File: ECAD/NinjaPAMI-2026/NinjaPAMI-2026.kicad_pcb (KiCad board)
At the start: 2 copper layers, 108 x 74 mm, 103 parts, among them J1 Con_Batt, J10 CON_EV_01, J11 Conn_01x04, J12 OLED, J13 RightMotor, J14 LeftMotor, J2 Servo, J3 Servo, J4 Sensor_RIGHT, J5 Sensor_Center, J6 Sensor_LEFT, J7 CON_EV_02, J8 CON_EV_02, J9 CON_PUMP_01, Q1 AO3400A, Q2 AO3400A, Q3 AO3400A, Q4 AO3400A, SW1 SW_SPDT, SW2 SW_Reed, SW3 SW_SPDT, U1 R-78E5.0-1.0, U2 XIAO-HALF-HOLE-23P, U3 TMC2209_SILENTSTEPSTICK, U4 TMC2209_SILENTSTEPSTICK

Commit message: placement pump and ev
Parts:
- C3, C4, J11: moved to B.Cu
- J12: footprint Connector_PinSocket_2.54mm:PinSocket_1x04_P2.54mm_Vertical -> Connector_Molex:Molex_KK-254_AE-6410-04A_1x04_P2.54mm_Vertical; moved to B.Cu
- moved kibuzzard-670C05E9 172.6 mm to (270.4, 106.2)
- moved kibuzzard-670C060B 159.6 mm to (267.4, 106.0)
- moved kibuzzard-670C0614 159.6 mm to (264.9, 105.7)
- moved kibuzzard-670C0418 154.9 mm to (273.9, 106.2)
- moved kibuzzard-670C0436 154.9 mm to (276.4, 106.2)
- moved kibuzzard-670C04A5 143.4 mm to (251.9, 93.2)
- moved G*** 143.4 mm to (254.5, 88.5)
- moved G*** 128.1 mm to (243.2, 93.4)
- moved G*** 109.4 mm to (247.0, 93.5)
- moved G*** 104.2 mm to (254.0, 104.5)
- moved kibuzzard-670C04A5 100.3 mm to (244.0, 89.5)
- moved G*** 100.3 mm to (241.4, 86.3)
- moved kibuzzard-670C23C9 100.0 mm to (258.0, 113.2)
- moved D10 94.9 mm to (168.0, 87.4)
- moved G*** 94.3 mm to (248.5, 88.8)
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
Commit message: modify ARU
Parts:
- removed SW1: SW_SPDT, PAMI-2025:UB16SKW03N-C
- added J15: BAU, Connector_Molex:Molex_KK-396_A-41791-0002_1x02_P3.96mm_Vertical, F.Cu at (116.4, 106.9)
- moved D10 37.2 mm to (205.2, 87.4)
- moved D11 37.2 mm to (205.2, 111.7)
- moved D14 37.2 mm to (214.5, 107.2)
- moved D3 37.2 mm to (205.3, 99.5)
- moved D4 37.2 mm to (214.5, 95.0)
- moved D6 37.2 mm to (205.0, 124.2)
- moved D7 37.2 mm to (214.2, 119.7)
- moved J10 37.2 mm to (220.0, 106.2)
- moved JP2 37.2 mm to (210.7, 97.5)
- moved JP3 37.2 mm to (210.5, 122.2)
- moved JP6 37.2 mm to (210.7, 109.7)
- moved Q1 37.2 mm to (210.3, 92.5)
- moved Q2 37.2 mm to (210.0, 117.2)
- moved Q4 37.2 mm to (210.2, 104.7)
- moved R10 37.2 mm to (204.0, 93.0)
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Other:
- outline, holes or cut-outs redrawn

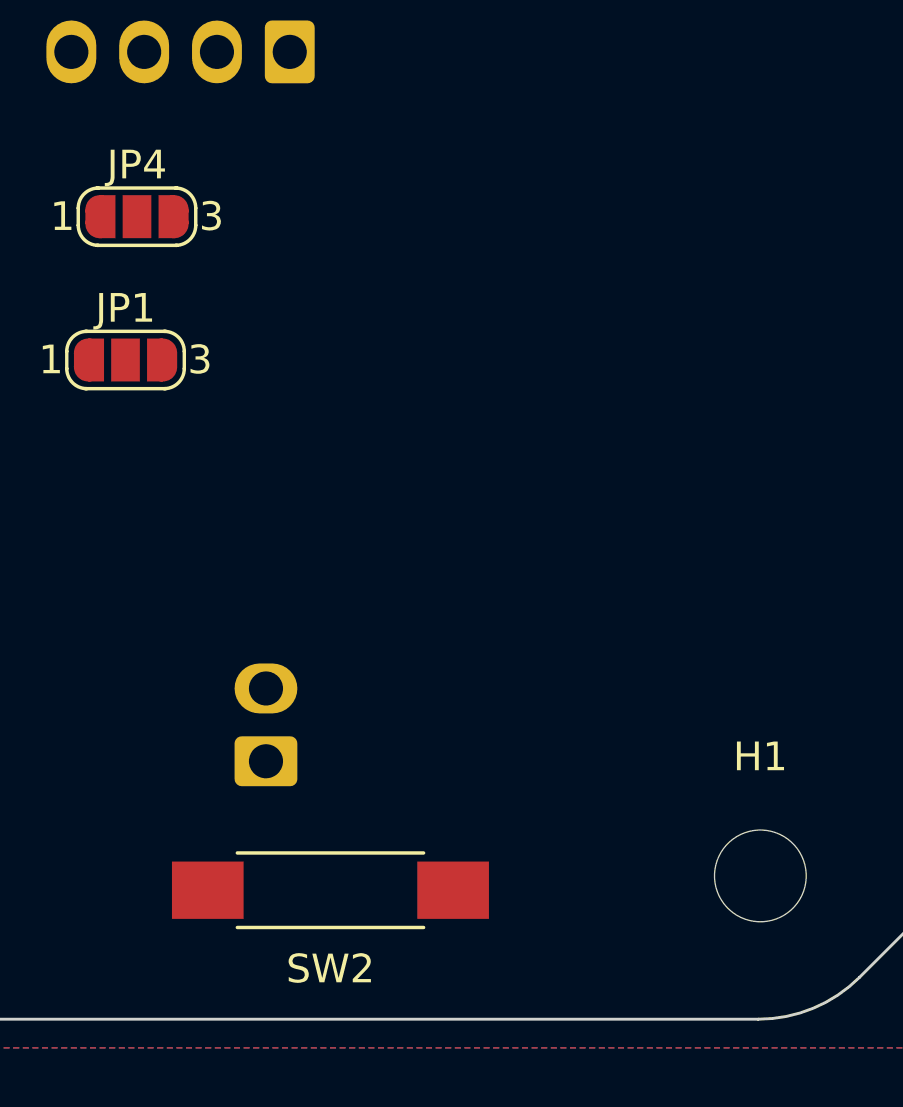
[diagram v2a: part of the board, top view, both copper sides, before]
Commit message: add hall effect sensor
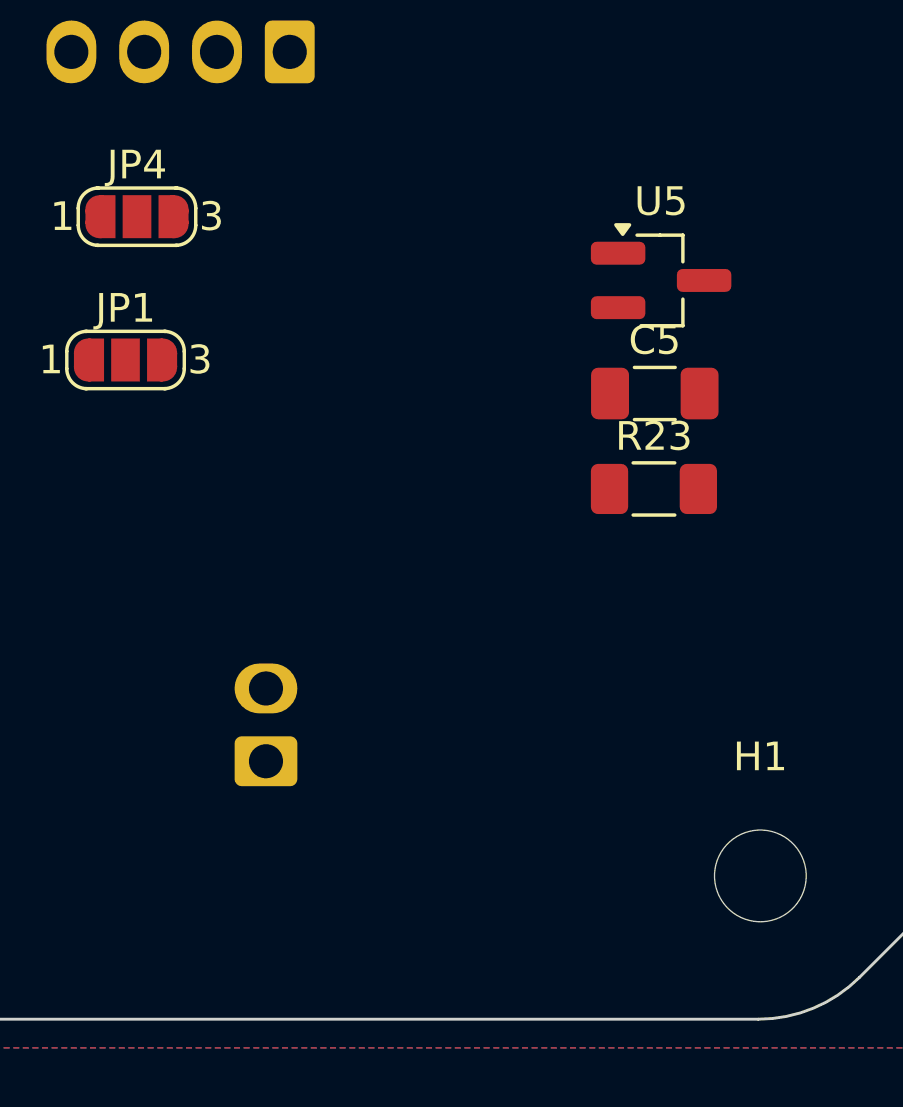
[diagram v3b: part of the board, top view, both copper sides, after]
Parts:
- removed SW2: SW_Reed, Button_Switch_SMD:SW_SPST_REED_CT05-XXXX-G1
- added C5: 0.1uF, Capacitor_SMD:C_1206_3216Metric_Pad1.33x1.80mm_HandSolder, F.Cu at (171.3, 117.2)
- added R23: 10K, Resistor_SMD:R_1206_3216Metric_Pad1.30x1.75mm_HandSolder, F.Cu at (171.3, 120.5)
- added U5: DRV5023, Package_TO_SOT_SMD:SOT-23_Handsoldering, F.Cu at (171.5, 113.2)

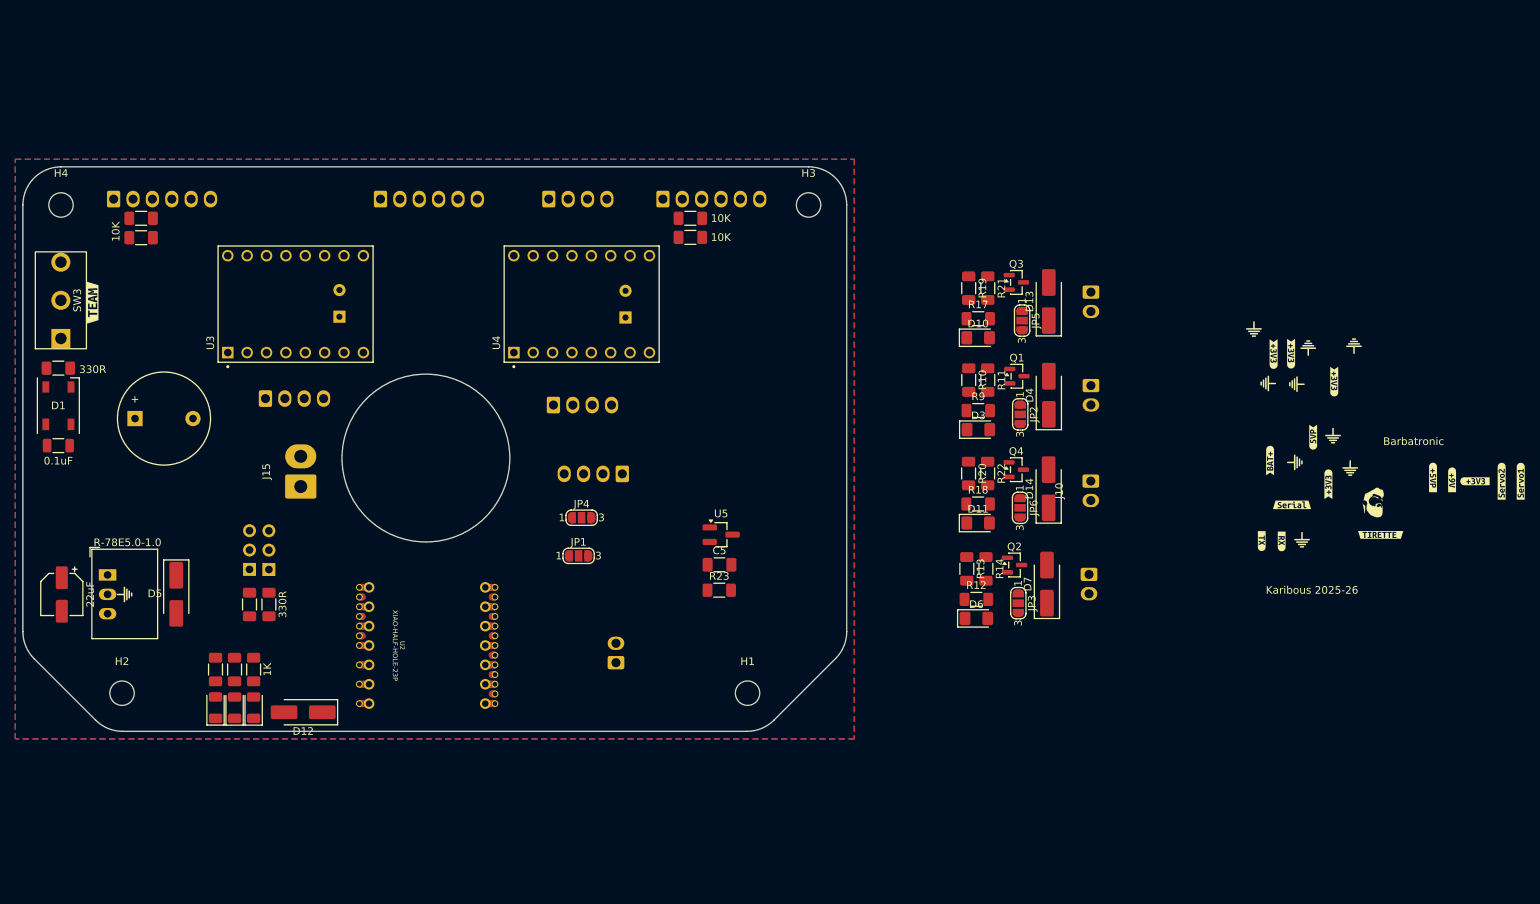
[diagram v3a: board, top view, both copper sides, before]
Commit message: size refactor - add 2.0 regulator
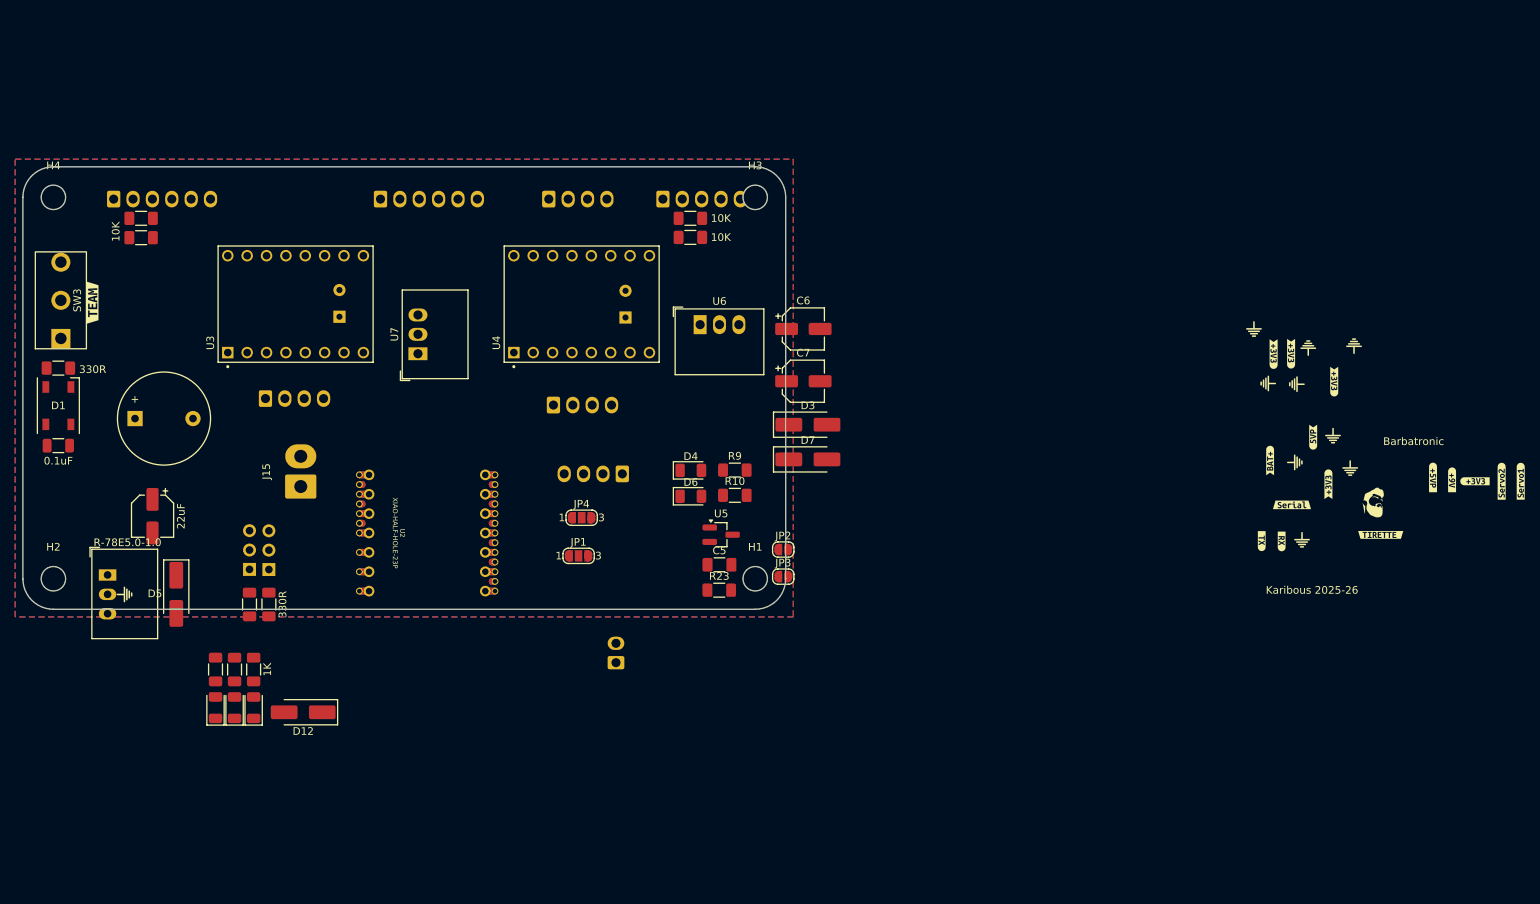
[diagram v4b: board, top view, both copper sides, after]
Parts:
- removed D10, D11: LED_Small, LED_SMD:LED_1206_3216Metric_Pad1.42x1.75mm_HandSolder
- removed D13, D14: D_Small, Diode_SMD:D_SMA_Handsoldering
- removed J10: CON_EV_01, Connector_Molex:Molex_KK-254_AE-6410-02A_1x02_P2.54mm_Vertical
- removed J7, J8: CON_EV_02, Connector_Molex:Molex_KK-254_AE-6410-02A_1x02_P2.54mm_Vertical
- removed J9: CON_PUMP_01, Connector_Molex:Molex_KK-254_AE-6410-02A_1x02_P2.54mm_Vertical
- removed JP5, JP6: SolderJumper_3_Open, Jumper:SolderJumper-3_P1.3mm_Open_RoundedPad1.0x1.5mm_NumberLabels
- removed Q1, Q2, Q3, Q4: AO3400A, Package_TO_SOT_SMD:SOT-23
- removed R11, R14, R21, R22: 10K, Resistor_SMD:R_1206_3216Metric_Pad1.30x1.75mm_HandSolder
- removed R12, R17, R18: 1K, Resistor_SMD:R_1206_3216Metric_Pad1.30x1.75mm_HandSolder
- removed R13, R19, R20: 270R, Resistor_SMD:R_1206_3216Metric_Pad1.30x1.75mm_HandSolder
- added C6: 22uF, Capacitor_SMD:CP_Elec_5x5.4, F.Cu at (182.3, 86.3)
- added C7: 22uF, Capacitor_SMD:CP_Elec_5x5.4, F.Cu at (182.3, 93.1)
- added U6: R-78B5.0-2.0, Converter_DCDC:Converter_DCDC_RECOM_R-78B-2.0_THT, F.Cu at (168.8, 85.7)
- added U7: R-78B5.0-2.0, Converter_DCDC:Converter_DCDC_RECOM_R-78B-2.0_THT, F.Cu at (131.8, 89.5)
- D3: value LED_Small -> D_Small; footprint LED_SMD:LED_1206_3216Metric_Pad1.42x1.75mm_HandSolder -> Diode_SMD:D_SMA_Handsoldering
- D4: value D_Small -> Green; footprint Diode_SMD:D_SMA_Handsoldering -> LED_SMD:LED_1206_3216Metric
- D6: value LED_Small -> Green; footprint LED_SMD:LED_1206_3216Metric_Pad1.42x1.75mm_HandSolder -> LED_SMD:LED_1206_3216Metric
- JP2, JP3: value SolderJumper_3_Open -> SolderJumper_2_Open; footprint Jumper:SolderJumper-3_P1.3mm_Open_RoundedPad1.0x1.5mm_NumberLabels -> Jumper:SolderJumper-2_P1.3mm_Open_RoundedPad1.0x1.5mm
- R10: value 270R -> 1K
- moved D4 48.0 mm to (167.6, 104.8), turned to 0 degrees
- moved D6 40.7 mm to (167.6, 108.2)
- moved JP2 35.8 mm to (179.7, 115.2), turned to 0 degrees
- moved D7 35.3 mm to (182.9, 103.4), turned to 0 degrees
- moved R10 34.2 mm to (173.3, 108.1), turned to 0 degrees
- moved R9 32.8 mm to (173.3, 104.8)
- moved JP3 31.0 mm to (179.7, 118.7), turned to 0 degrees
- moved D3 22.4 mm to (182.9, 98.8)
- moved H2 17.5 mm to (84.0, 119.0)
- moved C2 15.7 mm to (97.0, 110.8)
- moved H1 15.0 mm to (176.0, 119.0)
- moved U2 14.8 mm to (133.0, 113.0)
- moved H3 7.07 mm to (176.0, 69.0)
- moved H4 1.41 mm to (84.0, 69.0)
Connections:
- D12 pad 2: +5VP -> +5VL
- D3 pad 1: GND -> +9V
- D3 pad 2: Net-(D3-A) -> +5VP
- D4 pad 1: Net-(D4-K) -> GND
- D5 pad 2: +5VP -> +5VL
- D7 pad 1: Net-(D7-K) -> +9V
- D7 pad 2: Net-(D7-A) -> +5VD
- JP2 pad 1: +9V -> +3.3V
- JP2 pad 2: Net-(D4-K) -> LeftMS1
- JP3 pad 1: +9V -> +3.3V
- JP3 pad 2: Net-(D7-K) -> LeftMS2
- R10 pad 1: Net-(Q1-G) -> Net-(D6-A)
- R10 pad 2: S_PUMP_02 -> +5VL
- R9 pad 1: S_PUMP_02 -> Net-(D4-A)
- R9 pad 2: Net-(D3-A) -> +5VD
- U1 pad 3: +5VP -> +5VL
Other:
- board size 108 x 74 mm -> 100 x 58 mm

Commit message: routing and silkscreen
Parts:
- removed the G*** at (243.2, 93.4)
- removed the G*** at (247.0, 93.5)
- removed the G*** at (254.0, 104.5)
- removed the G*** at (246.8, 103.8)
- removed the G*** at (251.8, 100.2)
- removed the G*** at (247.7, 113.9)
- removed kibuzzard-670C0418: G***, kibuzzard-670C0418
- removed kibuzzard-670C0436: G***, kibuzzard-670C0436
- removed kibuzzard-670C045B: G***, kibuzzard-670C045B
- removed the kibuzzard-670C04A5 at (246.2, 89.5)
- removed the kibuzzard-670C04A5 at (244.0, 89.5)
- removed the kibuzzard-670C04A5 at (251.1, 106.6)
- removed the kibuzzard-670C04A5 at (251.9, 93.2)
- removed kibuzzard-670C05E9: G***, kibuzzard-670C05E9
- removed kibuzzard-670C060B: G***, kibuzzard-670C060B
- removed kibuzzard-670C0614: G***, kibuzzard-670C0614
- removed kibuzzard-670C077D: G***, kibuzzard-670C077D
- added G***: LOGO, LOGO, F.Cu at (126.2, 71.2)
- added G***: LOGO, LOGO, F.Cu at (133.1, 81.0)
- added G***: LOGO, LOGO, F.Cu at (96.1, 71.3)
- added G***: LOGO, LOGO, B.Cu at (101.1, 95.1)
- added G***: LOGO, LOGO, F.Cu at (147.9, 112.0)
- added G***: LOGO, LOGO, F.Cu at (113.7, 71.3)
- added G***: LOGO, LOGO, F.Cu at (158.5, 81.0)
- added G***: LOGO, LOGO, F.Cu at (156.1, 71.3)
- added G***: LOGO, LOGO, F.Cu at (103.1, 79.3)
- added J7: Conn_01x04, Connector_Molex:Molex_KK-254_AE-6410-04A_1x04_P2.54mm_Vertical, B.Cu at (108.4, 86.8)
- added J8: Conn_01x04, Connector_Molex:Molex_KK-254_AE-6410-04A_1x04_P2.54mm_Vertical, B.Cu at (101.1, 86.8)
- added JP5: SolderJumper_2_Open, Jumper:SolderJumper-2_P1.3mm_Open_RoundedPad1.0x1.5mm, F.Cu at (148.6, 90.1)
- added JP6: SolderJumper_2_Open, Jumper:SolderJumper-2_P1.3mm_Open_RoundedPad1.0x1.5mm, F.Cu at (148.6, 92.7)
- added kibuzzard-670C04A5: G***, kibuzzard-670C04A5, F.Cu at (153.6, 72.1)
- added kibuzzard-670C04A5: G***, kibuzzard-670C04A5, F.Cu at (111.2, 72.1)
- added kibuzzard-670C04A5: G***, kibuzzard-670C04A5, F.Cu at (123.6, 72.1)
- added kibuzzard-670C04A5: G***, kibuzzard-670C04A5, F.Cu at (93.7, 72.1)
- added kibuzzard-6998F5BE: G***, kibuzzard-6998F5BE, F.Cu at (108.7, 115.0)
- added kibuzzard-6998F5D7: G***, kibuzzard-6998F5D7, F.Cu at (96.8, 115.2)
- added kibuzzard-6998F8A6: G***, kibuzzard-6998F8A6, F.Cu at (111.1, 81.8)
- added kibuzzard-6998F8A6: G***, kibuzzard-6998F8A6, F.Cu at (103.8, 81.8)
- added kibuzzard-6998F8DE: G***, kibuzzard-6998F8DE, F.Cu at (108.4, 89.3)
- added kibuzzard-6998F8EA: G***, kibuzzard-6998F8EA, F.Cu at (101.1, 89.3)
- added kibuzzard-6998F900: G***, kibuzzard-6998F900, F.Cu at (103.4, 84.3)
- added kibuzzard-6998F900: G***, kibuzzard-6998F900, F.Cu at (110.8, 84.3)
- added kibuzzard-6998F92F: G***, kibuzzard-6998F92F, F.Cu at (111.3, 86.8)
- added kibuzzard-6998F92F: G***, kibuzzard-6998F92F, F.Cu at (103.9, 86.8)
- added kibuzzard-6998F94E: G***, kibuzzard-6998F94E, F.Cu at (102.4, 105.0)
- added kibuzzard-6998F94E: G***, kibuzzard-6998F94E, B.Cu at (102.3, 105.4)
- added kibuzzard-6998F954: G***, kibuzzard-6998F954, F.Cu at (99.8, 105.0)
- added kibuzzard-6998F954: G***, kibuzzard-6998F954, B.Cu at (99.8, 105.4)
- added kibuzzard-6998F9AD: G***, kibuzzard-6998F9AD, F.Cu at (104.8, 100.1)
- added kibuzzard-6998F9AD: G***, kibuzzard-6998F9AD, B.Cu at (102.3, 113.9)
- added kibuzzard-6998FA9D: G***, kibuzzard-6998FA9D, F.Cu at (118.0, 67.1)
- added kibuzzard-6998FA9D: G***, kibuzzard-6998FA9D, F.Cu at (130.4, 67.0)
- added kibuzzard-6998FA9D: G***, kibuzzard-6998FA9D, F.Cu at (160.4, 67.1)
- added kibuzzard-6998FA9D: G***, kibuzzard-6998FA9D, F.Cu at (100.4, 67.0)
- added kibuzzard-6998FAED: G***, kibuzzard-6998FAED, F.Cu at (103.0, 67.0)
- added kibuzzard-6998FAED: G***, kibuzzard-6998FAED, F.Cu at (120.6, 67.0)
- added kibuzzard-6998FAED: G***, kibuzzard-6998FAED, F.Cu at (163.0, 67.0)
- added kibuzzard-6998FAED: G***, kibuzzard-6998FAED, F.Cu at (132.9, 67.0)
- added kibuzzard-6998FB46: G***, kibuzzard-6998FB46, F.Cu at (108.1, 67.1)
- added kibuzzard-6998FB46: G***, kibuzzard-6998FB46, F.Cu at (168.0, 67.1)
- added kibuzzard-6998FB46: G***, kibuzzard-6998FB46, F.Cu at (138.1, 67.1)
- added kibuzzard-6998FE5D: G***, kibuzzard-6998FE5D, F.Cu at (126.2, 90.3)
- added kibuzzard-6998FE5D: G***, kibuzzard-6998FE5D, F.Cu at (151.4, 90.1)
- added kibuzzard-6998FE66: G***, kibuzzard-6998FE66, F.Cu at (151.4, 92.7)
- added kibuzzard-6998FE66: G***, kibuzzard-6998FE66, F.Cu at (126.2, 92.8)
- D3, D5, D7, G***, JP1, JP4, R10, R15, R5, R6, R9, kibuzzard-670C0798, kibuzzard-670C07A3: moved to B.Cu
- J11: moved to F.Cu
- J15: footprint Connector_Molex:Molex_KK-396_A-41791-0002_1x02_P3.96mm_Vertical -> Connector_Molex:Molex_KK-254_AE-6410-02A_1x02_P2.54mm_Vertical
- moved G*** 151.7 mm to (104.9, 113.5)
- moved G*** 141.3 mm to (104.4, 120.9)
- moved kibuzzard-670C047F 140.4 mm to (103.7, 116.6), turned to 45 degrees
- moved G*** 138.3 mm to (110.5, 79.3), turned to 90 degrees
- moved kibuzzard-670C0798 137.7 mm to (107.4, 113.7)
- moved kibuzzard-670C07A3 132.4 mm to (110.0, 113.6)
- moved G*** 114.1 mm to (142.9, 104.5)
- moved C6 98.9 mm to (84.1, 97.3), turned to 90 degrees
- moved C7 98.6 mm to (84.1, 85.1), turned to 90 degrees
- moved kibuzzard-670C23C9 91.6 mm to (166.6, 107.0), turned to -90 degrees
- moved D3 91.0 mm to (93.2, 83.3), turned to 90 degrees
- moved SW3 90.9 mm to (175.9, 80.9)
- moved C1 90.9 mm to (174.9, 90.2), turned to 0 degrees
- moved R7 90.7 mm to (174.9, 100.3), turned to 180 degrees
- moved D1 90.2 mm to (174.9, 95.4), turned to -90 degrees
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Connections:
- C5 pad 1: +3V3 -> +3.3V
- J11 pad 4: +5VP -> +5VD
- J12 pad 1: SDA -> +3.3V
- J12 pad 2: SCL -> GND
- J12 pad 3: +3.3V -> SCL
- J12 pad 4: GND -> SDA
- J2 pad 2: +5VP -> +5VD
- J3 pad 2: +5VP -> +5VD
- JP2 pad 2: LeftMS1 -> RightMS1
- JP3 pad 2: LeftMS2 -> RightMS2
- R23 pad 2: +3V3 -> +3.3V
- U2 pad 1: unconnected-(U2-GPIO1_D0/A0-Pad1) -> Buzzer
- U2 pad 10: unconnected-(U2-GPIO8_D9/A9/MISO-Pad10) -> S_PUMP_02
- U2 pad 11: unconnected-(U2-GPIO9_D10/A10/MOSI-Pad11) -> Servo02
- U2 pad 15: unconnected-(U2-GPIO38_DVP_VSYNC/I2S_SD-Pad15) -> Tirette
- U2 pad 16: unconnected-(U2-GPIO39_CAM_SCL/I2S_SCK-Pad16) -> Color_Team
- U2 pad 17: unconnected-(U2-GPIO40_CAM_SDA/I2S_WS-Pad17) -> LeftDir
- U2 pad 18: unconnected-(U2-GPIO41_PDM_DATA/RX1-Pad18) -> RightDir
- U2 pad 19: unconnected-(U2-GPIO42_PDM_CLK/TX1-Pad19) -> RightStep
- U2 pad 2: unconnected-(U2-GPIO2_D1/A1-Pad2) -> LED_Status
- U2 pad 20: unconnected-(U2-GPIO10_XMCLK/ADC_BAT-Pad20) -> XSHUT_CENTER
- U2 pad 21: unconnected-(U2-GPIO11_DVP_Y8/SPI_MOSI1-Pad21) -> S_PUMP_01
- U2 pad 22: unconnected-(U2-GPIO12_DVP_Y7/SPI_MISO1-Pad22) -> S_EV_02
- U2 pad 23: unconnected-(U2-GPIO13_DVP_PCLK/SPI_SCK1-Pad23) -> Servo01
- U2 pad 3: unconnected-(U2-GPIO3_D2/A2-Pad3) -> LeftStep
- U2 pad 4: unconnected-(U2-GPIO4_D3/A3-Pad4) -> EnDriver
- U2 pad 9: unconnected-(U2-GPIO7_D8/A8/SCK-Pad9) -> S_EV_01
- U3 pad 14: LeftMS2 -> RightMS2
- U3 pad 15: LeftMS1 -> RightMS1
- U5 pad 1: +3V3 -> +3.3V
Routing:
- net +3.3V: track 0.00 -> 312.3 mm
- net SCL: track 0.00 -> 133.8 mm, vias 0 -> 1
- net +9V: track 0.00 -> 133.4 mm
- net SDA: track 0.00 -> 133.3 mm
- net XSHUT_RIGHT: track 0.00 -> 60.0 mm, vias 0 -> 1
- net EnDriver: track 0.00 -> 58.3 mm
- net Color_Team: track 0.00 -> 58.3 mm
- net Tirette: track 0.00 -> 47.1 mm
- net XSHUT_LEFT: track 0.00 -> 44.0 mm, vias 0 -> 2
- net LED_Status: track 0.00 -> 42.2 mm
- net XSHUT_CENTER: track 0.00 -> 37.8 mm
- net +5VD: track 0.00 -> 37.7 mm
- net TX: track 0.00 -> 35.7 mm
- net S_EV_02: track 0.00 -> 33.9 mm
- net LeftStep: track 0.00 -> 33.7 mm
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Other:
- outline, holes or cut-outs redrawn
- board text added: "Produced by Aisler"

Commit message: fix driver inverted issue
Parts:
- J13: value RightMotor -> LeftMotor
- J14: value LeftMotor -> RightMotor
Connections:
- JP2 pad 2: RightMS1 -> LeftMS1
- JP3 pad 2: RightMS2 -> LeftMS2
- JP5 pad 2: LeftMS1 -> RightMS1
- JP6 pad 2: LeftMS2 -> RightMS2
- U2 pad 17: LeftDir -> RightStep
- U2 pad 18: RightDir -> LeftStep
- U2 pad 19: RightStep -> LeftDir
- U2 pad 3: LeftStep -> RightDir
- U3 pad 10: RightDir -> LeftStep
- U3 pad 14: RightMS2 -> LeftMS2
- U3 pad 15: RightMS1 -> LeftMS1
- U3 pad 9: RightStep -> LeftDir
- U4 pad 10: LeftDir -> RightStep
- U4 pad 14: LeftMS2 -> RightMS2
- U4 pad 15: LeftMS1 -> RightMS1
- U4 pad 9: LeftStep -> RightDir
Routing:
- net RightDir: track 18.6 -> 33.7 mm
- net LeftStep: track 33.7 -> 18.6 mm
- net RightStep: track 15.7 -> 30.0 mm
- net LeftDir: track 30.0 -> 15.7 mm
